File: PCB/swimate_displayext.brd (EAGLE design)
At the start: 69.5 x 34.3 mm, 55 parts, among them IC1 LPC11U24, T1 BSS84, T2 BSS84, U1 USD-SOCKETNEW, U5 DS3231MZ/V+T, U6 MAX1595EUA33+, U7 MAX1811ESA-T, U8 MAX16054AZT+T, U9 HC_05, Y1 12.000MHz

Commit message: Almost finished
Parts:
- removed R2: 2k, SparkFun-Passives:0805
- removed R8: 24k, SparkFun-Passives:0805
- added DISP: (no value), microbuilder:JSTPH8
- added SJ4: SOLDERJUMPERNC2, SparkFun-Passives:SJ_2S-NOTRACE
- LED2: device SparkFun-LED:LED-1206 -> SparkFun-LED:LED-0603
- moved JTAG1 58.9 mm to (4.83, 24.6), turned to 270 degrees
- moved J2 49.9 mm to (46.0, 2.54), turned to 180 degrees
- moved R4 48.9 mm to (2.79, 33.3), flipped to the bottom, turned to 0 degrees
- moved R3 48.8 mm to (3.05, 31.2), turned to 180 degrees
- moved U5 42.0 mm to (6.35, 14.0), flipped to the top
- moved C14 40.7 mm to (46.0, 9.91), turned to 180 degrees
- moved R1 35.4 mm to (38.6, 6.10)
- moved R7 35.2 mm to (47.8, 14.2), turned to 180 degrees
- moved SJ2 34.2 mm to (35.6, 44.5), turned to 0 degrees
- moved T2 34.0 mm to (30.5, 41.9)
- moved C9 33.8 mm to (10.7, 12.7), flipped to the top
- moved R13 33.2 mm to (36.1, 4.32)
- moved JP3 32.9 mm to (30.5, 1.27), turned to 0 degrees
- moved LED2 32.7 mm to (50.0, 15.0)
- moved U9 32.6 mm to (40.6, 41.9), turned to 90 degrees
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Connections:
- net N$17 renamed USBD_P
- net N$18 renamed USBD_N
- net SWCLK renamed SCK0
- removed net MPU_AD0: JP2.7, U2.9
- removed net N$12: C12.1, U6.1, U6.8
- removed net N$21: R2.2, SJ5.1
- removed net N$4: C5.1, U2.13, U2.3
- removed net N$6: C23.1, C24.1, C25.1, C26.1, IC1.10, IC1.33, IC1.48, IC1.58
- removed net VBATTMON: R1.1, R13.2
- new net DISP_CS: DISP.5
- new net DISP_DC: DISP.7
- new net VBATMON: IC1.40, R1.1, R13.2
- net 3.3V: now also C12.1, C23.1, C24.1, C25.1, C26.1, C5.1, DISP.2, IC1.10, IC1.33, IC1.48, IC1.58, U2.13, U2.3, U6.1, U6.8; no longer JP2.1
- net GND: now also DISP.8, JP2.7, SJ4.1, SJ5.1, U2.1, U2.11, U2.9; no longer R2.1, R8.2, SW_MODE.P$1, SW_PWR.P$1
- net N$1: no longer SW_PWR.P$3
- net RST: now also DISP.3
- net SPI0_MOSI: now also DISP.6
- net SPI0_SCK: now also DISP.4
- net SW_MODE: no longer SW_MODE.P$3
- net SYS_SHUTDOWN: now also SJ4.2; no longer R8.1
- net VBAT: now also C15.1, DISP.1, JP2.1, U8.6
- net VUSB: no longer C15.1, U8.6
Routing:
- net 3.3V: track 12.9 -> 168.4 mm, vias 0 -> 5
- net GND: track 185.2 -> 316.7 mm
- net VBAT: track 26.7 -> 109.6 mm, vias 0 -> 5
- net RST: track 0.00 -> 73.9 mm, vias 0 -> 2
- net N$6: track 37.4 -> 0.00 mm, vias 1 -> 0
- net VBATMON: track 0.00 -> 35.3 mm, vias 0 -> 2
- net SWDIO: track 0.00 -> 34.7 mm
- net MCU_RX: track 0.00 -> 28.1 mm, vias 0 -> 1
- net N$15: track 27.2 -> 0.00 mm, vias 1 -> 0
- net 3V3_ENABLE: track 26.8 -> 0.00 mm, vias 1 -> 0
- net MCU_TX: track 0.00 -> 26.1 mm, vias 0 -> 1
- net VUSB: track 27.2 -> 49.9 mm, vias 0 -> 3
- net I2C_SDA: track 20.8 -> 42.4 mm, vias 2 -> 3
- net USBD_P: track 31.3 -> 14.3 mm
- net USBD_N: track 28.0 -> 11.2 mm
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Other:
- board size 69.5 x 34.3 mm -> 50.8 x 50.8 mm

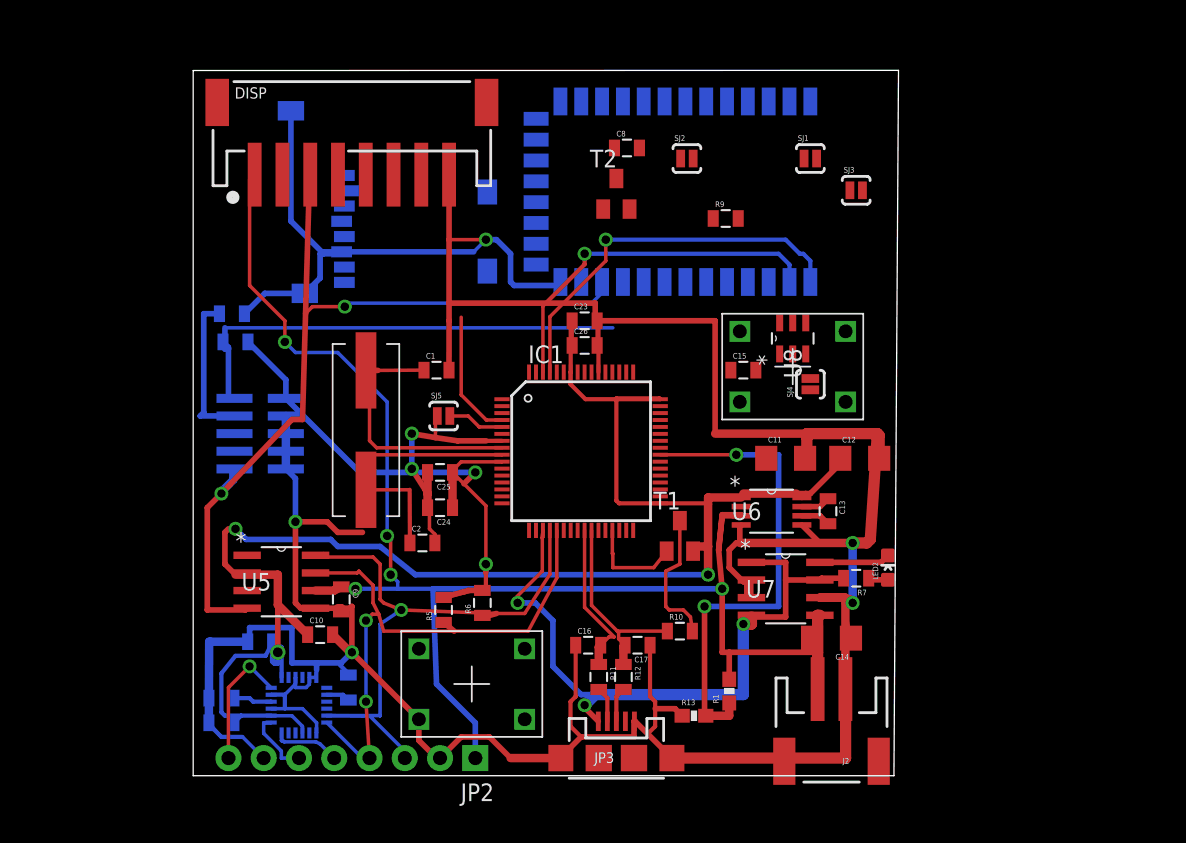
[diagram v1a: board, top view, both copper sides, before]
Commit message: Passed DRC
TODO: DRC, connect CS signals for display and SD card.
TODO: replace connector for display board.
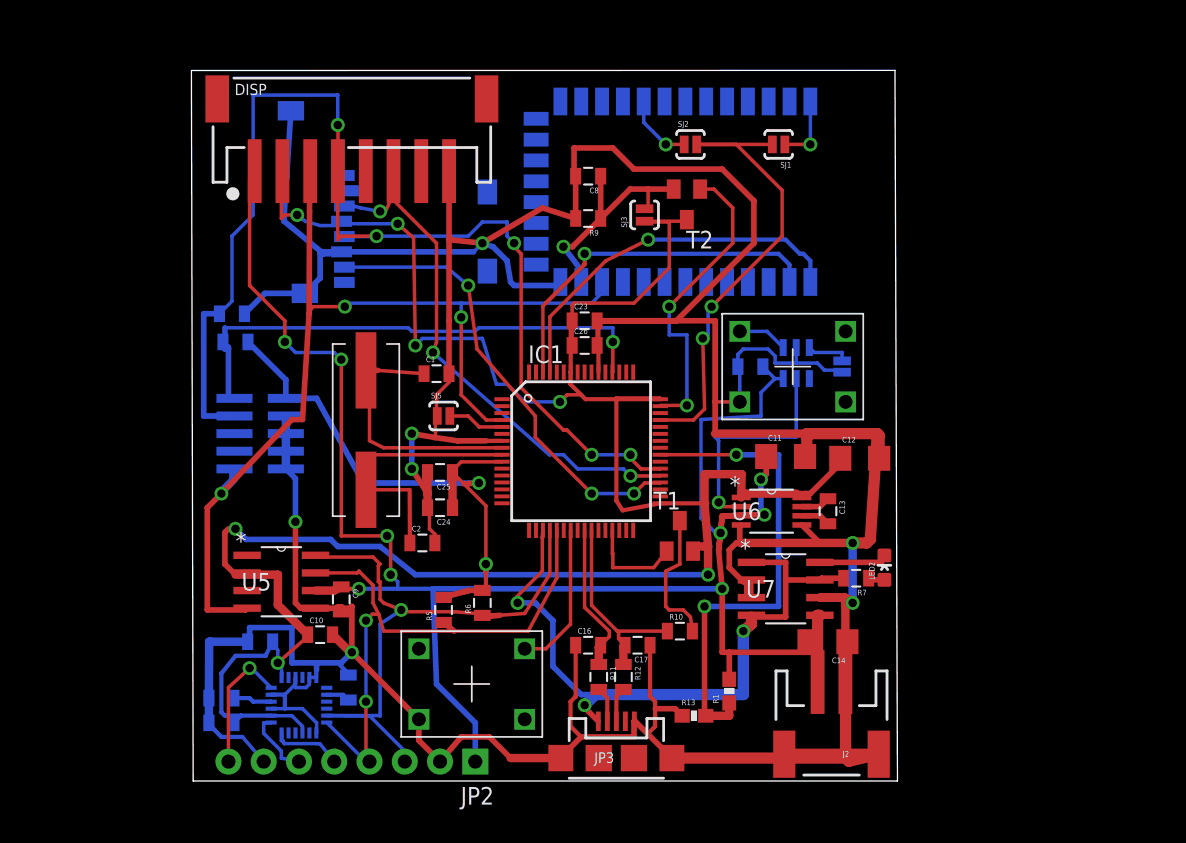
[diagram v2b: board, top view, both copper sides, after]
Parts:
- moved SJ3 15.3 mm to (32.5, 40.4), turned to 90 degrees
- moved R9 9.91 mm to (28.4, 40.1), turned to 180 degrees
- moved T2 5.14 mm to (35.6, 41.1), turned to 180 degrees
- moved C8 3.45 mm to (28.4, 43.2), turned to 180 degrees
- moved SJ4 2.62 mm to (46.7, 29.5), flipped to the bottom
- moved SJ1 2.50 mm to (42.2, 45.5), turned to 180 degrees
- moved U8 1.80 mm to (43.4, 29.7), flipped to the bottom, turned to 270 degrees
- moved SJ2 1.05 mm to (35.8, 45.5)
- moved C15 0.57 mm to (40.1, 29.5), flipped to the bottom
- moved J2 0.51 mm to (46.0, 3.05)
- moved C14 0.36 mm to (45.7, 9.65)
- moved C1 0.25 mm to (17.5, 29.0)
- moved JP2 0.25 mm to (20.3, 1.02)
- moved DISP 0.25 mm to (11.4, 47.2)
- moved LED2 0.25 mm to (49.8, 15.0)
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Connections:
- removed net SCK0: IC1.38, JTAG1.4, R4.2
- net BT_ENABLE: now also IC1.47
- net BT_KEY: now also IC1.45
- net GND: now also J2.NC1, J2.NC2
- net SPI0_SCK: now also IC1.38, JTAG1.4, R4.2
- net SW_MODE: now also IC1.23, SW_MODE.P$3; no longer SW_MODE.P$4
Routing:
- net SPI0_SCK: track 0.00 -> 84.0 mm, vias 0 -> 5
- net 3.3V: track 168.4 -> 225.6 mm, vias 5 -> 9
- net GND: track 316.7 -> 371.9 mm
- net SPI0_MOSI: track 0.00 -> 38.7 mm, vias 0 -> 3
- net BT_KEY: track 0.00 -> 34.7 mm, vias 0 -> 2
- net SPI0_MISO: track 0.00 -> 33.0 mm, vias 0 -> 3
- net VBAT: track 109.6 -> 136.0 mm, vias 5 -> 9
- net BT_ENABLE: track 0.00 -> 22.2 mm, vias 0 -> 2
- net N$15: track 0.00 -> 17.5 mm, vias 0 -> 1
- net 3V3_ENABLE: track 0.00 -> 16.7 mm, vias 0 -> 1
- net SCK0: track 11.1 -> 0.00 mm
- net SW_MODE: track 0.00 -> 10.8 mm
- net N$9: track 0.00 -> 5.08 mm, vias 0 -> 1
- net N$11: track 0.00 -> 4.93 mm, vias 0 -> 1
- net N$1: track 0.00 -> 3.61 mm
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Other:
- board size 50.8 x 50.8 mm -> 50.9 x 51.2 mm

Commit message: Added CS pins and turn off logic (MCU safe powerdown for SD card
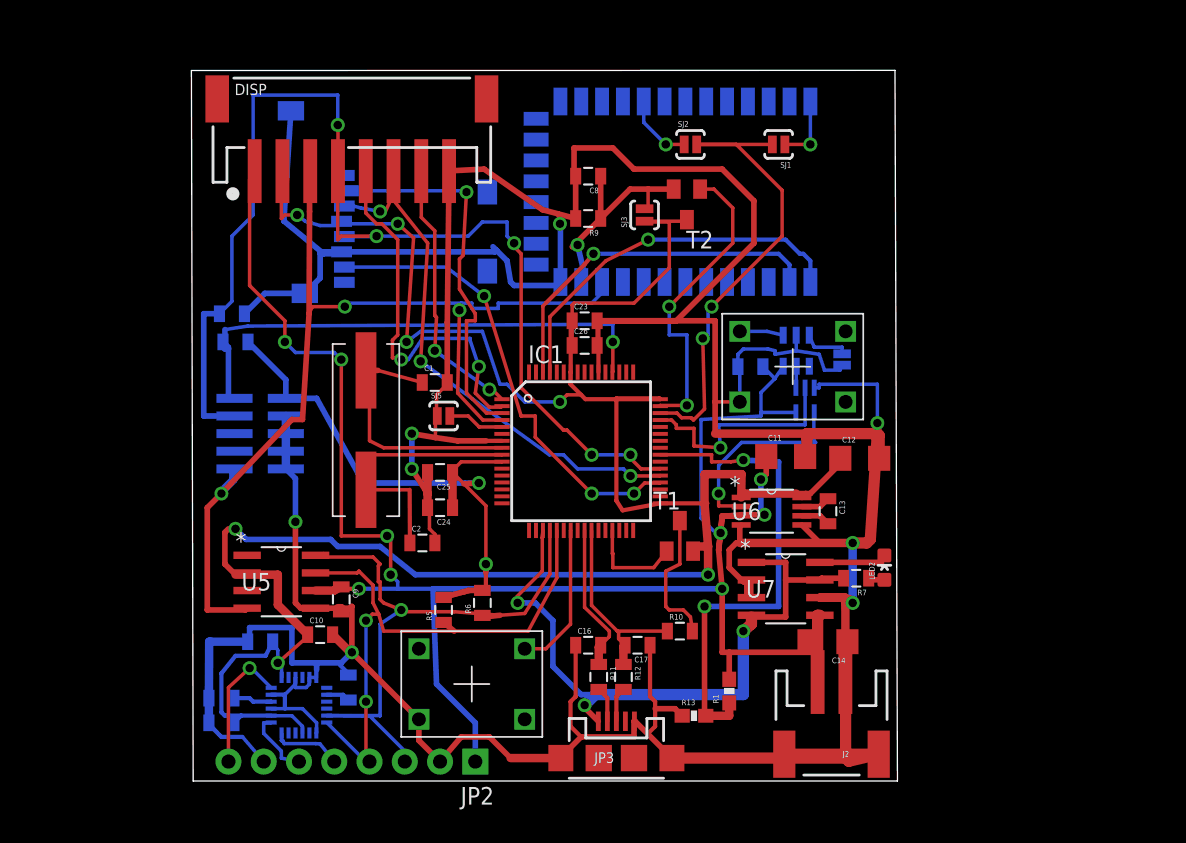
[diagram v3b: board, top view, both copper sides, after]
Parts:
- added U3: NC7SV86P5X, Fairchild_By_element14_Batch_1:SOT65P210X110-5N
- moved U8 0.89 mm to (43.4, 30.6)
- moved C1 0.65 mm to (17.4, 28.3)
- moved SJ4 0.51 mm to (46.7, 30.0)
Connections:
- new net N$2: U3.1, U8.5
- new net PO_DISABLE: IC1.45, U3.2
- net 3V3_ENABLE: now also U3.4; no longer U8.5
- net BT_KEY: now also IC1.46; no longer IC1.45
- net DISP_CS: now also IC1.2
- net DISP_DC: now also IC1.1
- net GND: now also U3.3
- net SD_CS: now also IC1.3
- net VBAT: now also U3.5
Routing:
- net DISP_CS: track 0.00 -> 27.7 mm, vias 0 -> 2
- net SD_CS: track 0.00 -> 27.1 mm, vias 0 -> 1
- net DISP_DC: track 0.00 -> 19.4 mm, vias 0 -> 2
- net PO_DISABLE: track 0.00 -> 16.6 mm, vias 0 -> 1
- net GND: track 371.9 -> 386.1 mm, vias 7 -> 8
- net VBAT: track 136.0 -> 139.0 mm
- net 3V3_ENABLE: track 16.7 -> 14.5 mm
- net N$2: track 0.00 -> 1.57 mm
- net RST: track 75.2 -> 76.2 mm
- net 3.3V: track 225.6 -> 226.4 mm
- net N$15: track 17.5 -> 17.0 mm
